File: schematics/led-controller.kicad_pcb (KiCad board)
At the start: 2 copper layers, 88.9 x 97.8 mm, 70 parts, among them CON1 BARREL_JACK, IC1 ATMEGA168A-P, P1 VIN, P2 VOUT, P3 LED1, P4 CONN_01X02, P5 CONN_01X02, P6 CONN_01X02, P7 ISP, P8 COM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

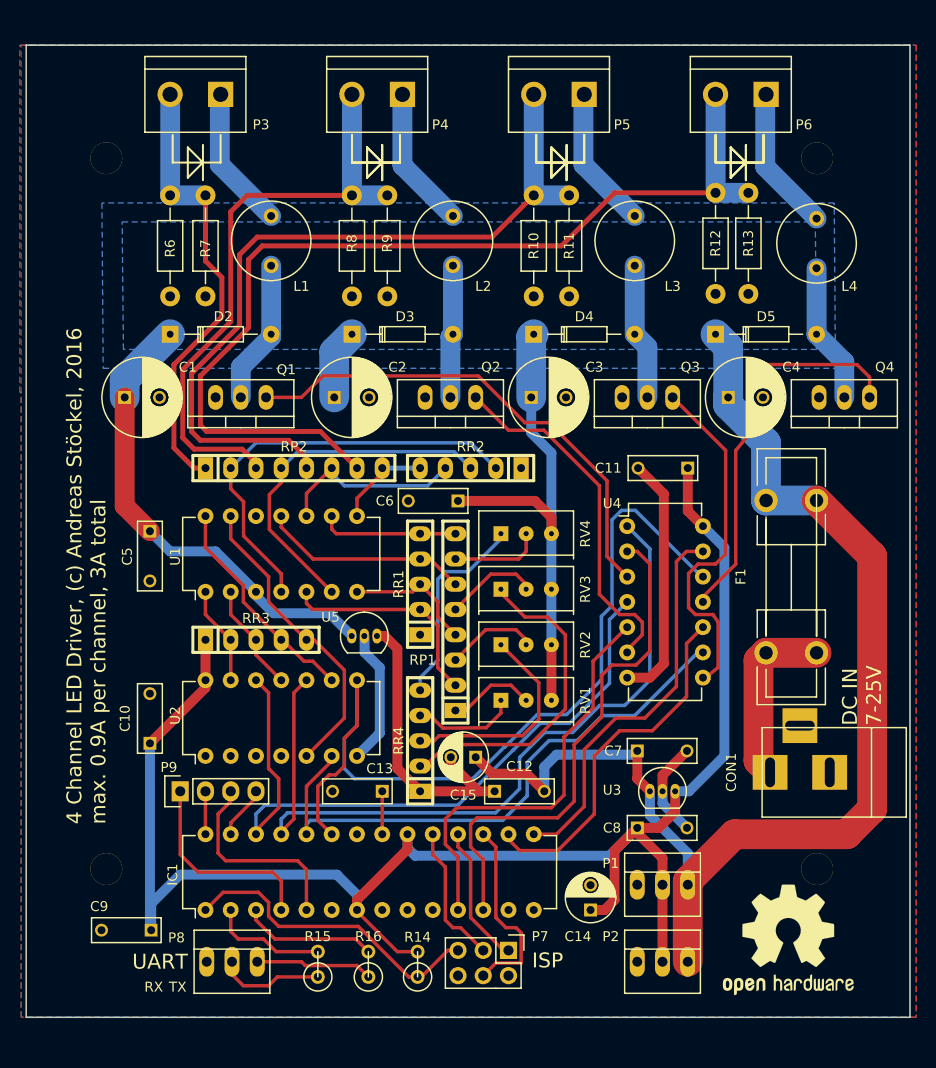
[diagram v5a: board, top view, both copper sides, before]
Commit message: Fixed small issues found on the produced board
- U3 was the wrong way round
- Holes for diodes could have been a little bigger
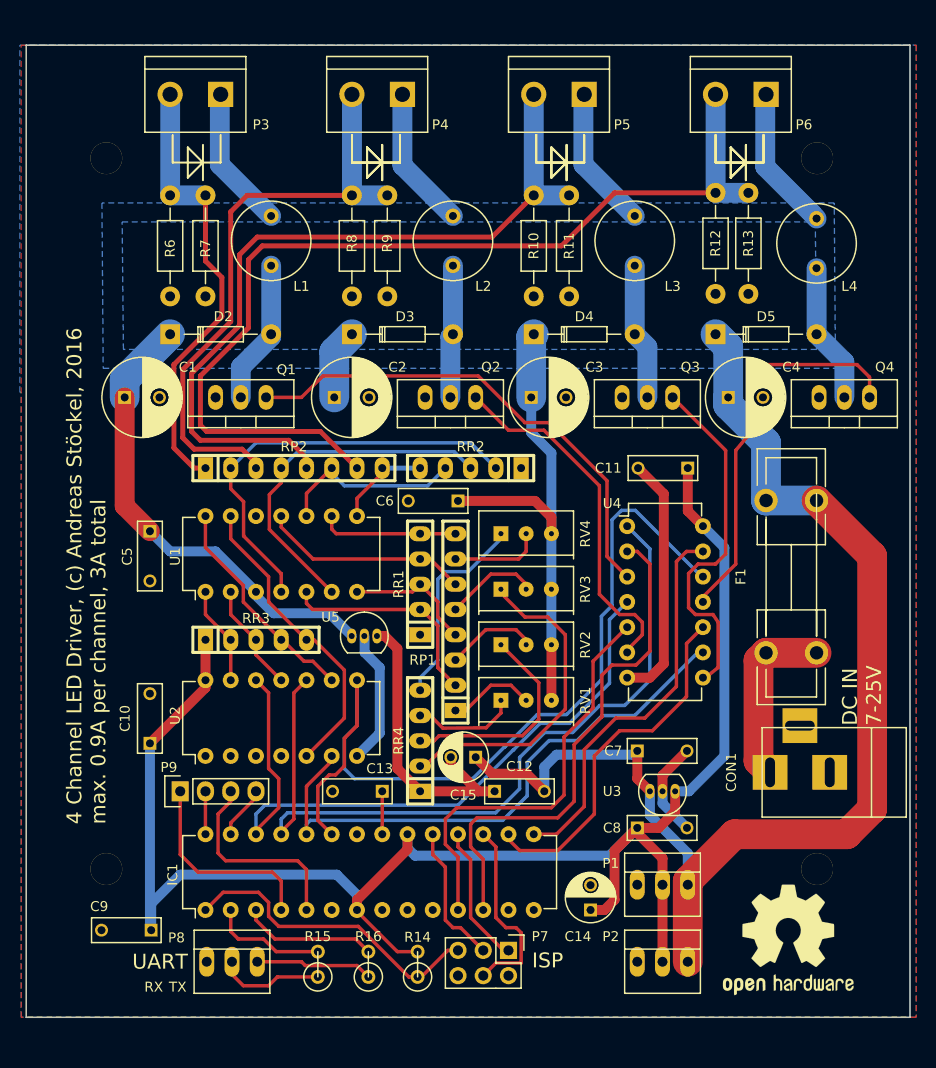
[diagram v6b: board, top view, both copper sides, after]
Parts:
- U3: value LP 2950 ACZ3,3 -> LP2950ACZ33
- moved U3 2.54 mm to (156.7, 105.5), turned to 180 degrees
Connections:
- U3 pad 1: VCC -> +3V3
- U3 pad 3: +3V3 -> VCC
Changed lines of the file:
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@@
   )
   (setup
-    (last_trace_width 1)
+    (last_trace_width 0.5)
     (user_trace_width 0.25)
     (user_trace_width 0.35)
@@
     (mod_text_size 1 1)
     (mod_text_width 0.15)
-    (pad_size 3.2 3.2)
-    (pad_drill 3.2)
+    (pad_size 2 2)
+    (pad_drill 1)
     (pad_to_mask_clearance 0.2)
     (aux_axis_origin 100.33 125.095)
@@
     (pcbplotparams
       (layerselection 0x010f0_80000001)
-      (usegerberextensions false)
+      (usegerberextensions true)
       (excludeedgelayer true)
       (linewidth 0.100000)
@@
       (psa4output false)
       (plotreference true)
-      (plotvalue true)
+      (plotvalue false)
       (plotinvisibletext false)
       (padsonsilk false)
@@
     (fp_line (start 7.36652 -0.76454) (end 2.79452 -0.76454) (layer F.SilkS) (width 0.15))
     (fp_line (start 2.79452 -0.76454) (end 2.79452 -0.00254) (layer F.SilkS) (width 0.15))
-    (pad 2 thru_hole circle (at 10.16052 -0.00254 180) (size 1.69926 1.69926) (drill 0.70104) (layers *.Cu *.Mask F.SilkS)
+    (pad 2 thru_hole circle (at 10.16052 -0.00254 180) (size 2 2) (drill 1) (layers *.Cu *.Mask F.SilkS)
       (net 34 "Net-(D2-Pad2)"))
-    (pad 1 thru_hole rect (at 0.00052 -0.00254 180) (size 1.69926 1.69926) (drill 0.70104) (layers *.Cu *.Mask F.SilkS)
+    (pad 1 thru_hole rect (at 0.00052 -0.00254 180) (size 2 2) (drill 1) (layers *.Cu *.Mask F.SilkS)
       (net 1 VCC))
     (model Diodes_ThroughHole.3dshapes/Diode_DO-35_SOD27_Horizontal_RM10.wrl
@@
     (fp_line (start 7.36652 -0.76454) (end 2.79452 -0.76454) (layer F.SilkS) (width 0.15))
     (fp_line (start 2.79452 -0.76454) (end 2.79452 -0.00254) (layer F.SilkS) (width 0.15))
-    (pad 2 thru_hole circle (at 10.16052 -0.00254 180) (size 1.69926 1.69926) (drill 0.70104) (layers *.Cu *.Mask F.SilkS)
+    (pad 2 thru_hole circle (at 10.16052 -0.00254 180) (size 2 2) (drill 1) (layers *.Cu *.Mask F.SilkS)
       (net 35 "Net-(D3-Pad2)"))
-    (pad 1 thru_hole rect (at 0.00052 -0.00254 180) (size 1.69926 1.69926) (drill 0.70104) (layers *.Cu *.Mask F.SilkS)
+    (pad 1 thru_hole rect (at 0.00052 -0.00254 180) (size 2 2) (drill 1) (layers *.Cu *.Mask F.SilkS)
       (net 1 VCC))
     (model Diodes_ThroughHole.3dshapes/Diode_DO-35_SOD27_Horizontal_RM10.wrl
@@
     (fp_line (start 7.36652 -0.76454) (end 2.79452 -0.76454) (layer F.SilkS) (width 0.15))
     (fp_line (start 2.79452 -0.76454) (end 2.79452 -0.00254) (layer F.SilkS) (width 0.15))
-    (pad 2 thru_hole circle (at 10.16052 -0.00254 180) (size 1.69926 1.69926) (drill 0.70104) (layers *.Cu *.Mask F.SilkS)
+    (pad 2 thru_hole circle (at 10.16052 -0.00254 180) (size 2 2) (drill 1) (layers *.Cu *.Mask F.SilkS)
       (net 36 "Net-(D4-Pad2)"))
-    (pad 1 thru_hole rect (at 0.00052 -0.00254 180) (size 1.69926 1.69926) (drill 0.70104) (layers *.Cu *.Mask F.SilkS)
+    (pad 1 thru_hole rect (at 0.00052 -0.00254 180) (size 2 2) (drill 1) (layers *.Cu *.Mask F.SilkS)
       (net 1 VCC))
     (model Diodes_ThroughHole.3dshapes/Diode_DO-35_SOD27_Horizontal_RM10.wrl
@@
     (fp_line (start 7.36652 -0.76454) (end 2.79452 -0.76454) (layer F.SilkS) (width 0.15))
     (fp_line (start 2.79452 -0.76454) (end 2.79452 -0.00254) (layer F.SilkS) (width 0.15))
-    (pad 2 thru_hole circle (at 10.16052 -0.00254 180) (size 1.69926 1.69926) (drill 0.70104) (layers *.Cu *.Mask F.SilkS)
+    (pad 2 thru_hole circle (at 10.16052 -0.00254 180) (size 2 2) (drill 1) (layers *.Cu *.Mask F.SilkS)
       (net 37 "Net-(D5-Pad2)"))
-    (pad 1 thru_hole rect (at 0.00052 -0.00254 180) (size 1.69926 1.69926) (drill 0.70104) (layers *.Cu *.Mask F.SilkS)
+    (pad 1 thru_hole rect (at 0.00052 -0.00254 180) (size 2 2) (drill 1) (layers *.Cu *.Mask F.SilkS)
       (net 1 VCC))
     (model Diodes_ThroughHole.3dshapes/Diode_DO-35_SOD27_Horizontal_RM10.wrl
@@
   )
   (module TO_SOT_Packages_THT:TO-92_Inline_Narrow_Oval (layer F.Cu)
-    (at 154.178 105.537)
+    (at 156.718 105.537 180)
     (descr "TO-92 leads in-line, narrow, oval pads, drill 0.6mm (see NXP sot054_po.pdf)")
     (tags "to-92 sc-43 sc-43a sot54 PA33 transistor")
-    (fp_text reference U3 (at -3.81 -0.127) (layer F.SilkS)
-      (effects (font (size 1 1) (thickness 0.15)))
-    )
-    (fp_text value "LP 2950 ACZ3,3" (at 0 3) (layer F.Fab)
+    (fp_text reference U3 (at 6.35 0 180) (layer F.SilkS)
+      (effects (font (size 1 1) (thickness 0.15)))
+    )
+    (fp_text value LP2950ACZ33 (at 0 3 180) (layer F.Fab)
       (effects (font (size 1 1) (thickness 0.15)))
     )
@@
     (fp_line (start -1.4 -2.65) (end 3.95 -2.65) (layer F.CrtYd) (width 0.05))
     (fp_line (start 3.95 1.95) (end 3.95 -2.65) (layer F.CrtYd) (width 0.05))
-    (pad 2 thru_hole oval (at 1.27 0 180) (size 0.89916 1.50114) (drill 0.6) (layers *.Cu *.Mask F.SilkS)
-      (net 2 GND))
-    (pad 3 thru_hole oval (at 2.54 0 180) (size 0.89916 1.50114) (drill 0.6) (layers *.Cu *.Mask F.SilkS)
+    (pad 2 thru_hole oval (at 1.27 0) (size 0.89916 1.50114) (drill 0.6) (layers *.Cu *.Mask F.SilkS)
+      (net 2 GND))
+    (pad 3 thru_hole oval (at 2.54 0) (size 0.89916 1.50114) (drill 0.6) (layers *.Cu *.Mask F.SilkS)
+      (net 1 VCC))
+    (pad 1 thru_hole oval (at 0 0) (size 0.89916 1.50114) (drill 0.6) (layers *.Cu *.Mask F.SilkS)
       (net 3 +3V3))
-    (pad 1 thru_hole oval (at 0 0 180) (size 0.89916 1.50114) (drill 0.6) (layers *.Cu *.Mask F.SilkS)
-      (net 1 VCC))
     (model TO_SOT_Packages_THT.3dshapes/TO-92_Inline_Narrow_Oval.wrl
       (at (xyz 0.05 0 0))
@@
   (segment (start 165.862 70.485) (end 165.862 76.28636) (width 3) (layer B.Cu) (net 1) (status 20))
   (segment (start 162.052 66.675) (end 165.862 70.485) (width 3) (layer B.Cu) (net 1))
-  (segment (start 154.178 105.537) (end 154.178 107.95) (width 1) (layer B.Cu) (net 1) (status 10))
   (segment (start 157.988 111.76) (end 157.988 114.554) (width 1) (layer B.Cu) (net 1) (status 20))
-  (segment (start 154.178 107.95) (end 157.988 111.76) (width 1) (layer B.Cu) (net 1))
   (segment (start 157.988 122.682) (end 157.988 114.554) (width 3) (layer F.Cu) (net 1) (status 30))
   (segment (start 157.988 114.554) (end 162.687 109.855) (width 3) (layer F.Cu) (net 1) (status 10))
@@
   (segment (start 176.53 81.87436) (end 170.942 76.28636) (width 3) (layer F.Cu) (net 1) (status 20))
   (segment (start 152.908 101.473) (end 152.908 104.267) (width 1) (layer F.Cu) (net 1) (status 10))
-  (segment (start 152.908 104.267) (end 154.178 105.537) (width 1) (layer F.Cu) (net 1) (status 20))
   (segment (start 144.78 101.854) (end 152.527 101.854) (width 1) (layer B.Cu) (net 1) (status 20))
   (segment (start 152.527 101.854) (end 152.908 101.473) (width 1) (layer B.Cu) (net 1) (status 30))
@@
   (segment (start 105.918 81.407) (end 110.49 81.407) (width 1) (layer B.Cu) (net 1))
   (segment (start 144.272 91.059) (end 144.272 96.393) (width 1) (layer F.Cu) (net 1) (status 30))
+  (segment (start 154.178 105.537) (end 154.178 107.95) (width 1) (layer B.Cu) (net 1) (status 10))
+  (segment (start 154.178 107.95) (end 157.988 111.76) (width 1) (layer B.Cu) (net 1))
+  (segment (start 152.908 104.267) (end 154.178 105.537) (width 1) (layer F.Cu) (net 1) (status 20))
   (segment (start 151.892 94.107) (end 154.178 94.107) (width 1) (layer F.Cu) (net 2) (status 10))
   (segment (start 155.575 75.612) (end 152.988 73.025) (width 1) (layer F.Cu) (net 2) (status 20))
@@
   (segment (start 127 99.695) (end 124.714 101.981) (width 1) (layer B.Cu) (net 2) (status 20))
   (segment (start 127 93.091) (end 127 99.695) (width 1) (layer B.Cu) (net 2))
-  (segment (start 103.886 100.711) (end 103.886 119.38) (width 1) (layer B.Cu) (net 3) (status C00000))
-  (segment (start 103.886 119.38) (end 104.013 119.507) (width 1) (layer B.Cu) (net 3) (status C00000))
-  (segment (start 104.013 119.507) (end 104.013 116.84) (width 1) (layer B.Cu) (net 3) (status 400000))
+  (segment (start 156.718 105.537) (end 158.115 105.537) (width 1) (layer B.Cu) (net 3) (status 10))
+  (segment (start 158.115 105.537) (end 161.671 101.981) (width 1) (layer B.Cu) (net 3))
+  (segment (start 156.718 107.569) (end 156.718 105.537) (width 1) (layer F.Cu) (net 3) (status 20))
+  (segment (start 103.886 100.711) (end 103.886 119.38) (width 1) (layer B.Cu) (net 3))
+  (segment (start 103.886 119.38) (end 104.013 119.507) (width 1) (layer B.Cu) (net 3))
+  (segment (start 104.013 119.507) (end 104.013 116.84) (width 1) (layer B.Cu) (net 3))
   (segment (start 104.013 116.84) (end 106.934 113.919) (width 1) (layer B.Cu) (net 3))
   (segment (start 148.209 117.475) (end 149.606 117.475) (width 1) (layer F.Cu) (net 3))
@@
   (segment (start 155.448 112.268) (end 152.908 109.728) (width 1) (layer F.Cu) (net 3) (status 20))
   (segment (start 152.908 109.728) (end 152.908 109.22) (width 1) (layer F.Cu) (net 3) (status 30))
-  (segment (start 156.718 105.537) (end 158.115 105.537) (width 1) (layer B.Cu) (net 3) (status 10))
   (segment (start 161.671 81.026) (end 159.512 78.867) (width 1) (layer B.Cu) (net 3) (status 20))
   (segment (start 161.671 101.981) (end 161.671 81.026) (width 1) (layer B.Cu) (net 3))
-  (segment (start 158.115 105.537) (end 161.671 101.981) (width 1) (layer B.Cu) (net 3))
   (segment (start 152.908 109.22) (end 155.067 109.22) (width 1) (layer F.Cu) (net 3) (status 10))
-  (segment (start 156.718 107.569) (end 156.718 105.537) (width 1) (layer F.Cu) (net 3) (status 20))
   (segment (start 155.067 109.22) (end 156.718 107.569) (width 1) (layer F.Cu) (net 3))
   (segment (start 152.908 109.22) (end 153.162 109.22) (width 1) (layer F.Cu) (net 3) (status 30))
